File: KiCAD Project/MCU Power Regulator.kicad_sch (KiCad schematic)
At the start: 0 parts

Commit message: V1.0.0.0
Final version 1, sent for fabrication.
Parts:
- added C3: 10µF, Capacitor_SMD:C_0603_1608Metric, symbol Device:C
- added C4: 100n, Capacitor_SMD:C_0603_1608Metric, symbol Device:C
- added C5: 3n3, Capacitor_SMD:C_0603_1608Metric, symbol Device:C
- added C6: 22µ, Capacitor_SMD:C_0603_1608Metric, symbol Device:C
- added L2: VLS5045EX-2R2N, VLS5045EX330M, symbol 1016:VLS5045EX-2R2N
- added R3: 100K, Resistor_SMD:R_0603_1608Metric, symbol Device:R_US
- added R4: 31K6, Resistor_SMD:R_0603_1608Metric, symbol Device:R_US
- added R5: 1K6, Resistor_SMD:R_0603_1608Metric, symbol Device:R_US
- added TP1: TestPoint, TestPoint:TestPoint_THTPad_D1.0mm_Drill0.5mm, symbol Connector:TestPoint
- added U1: TPS62130RGTR, QFN50P300X300X100-17N-D, symbol 1016:TPS62130RGTR
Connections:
- net GND: now also C3.2, C4.2, C5.1, C6.2, R4.2, R5.1, U1.15 (PGND_1), U1.16 (PGND_2), U1.17 (EP), U1.6 (AGND), U1.8 (DEF)
- net VCC: now also C3.1, C4.1, U1.10 (AVIN), U1.11 (PVIN_1), U1.12 (PVIN_2), U1.13 (EN), U1.7 (FSW)
- new net MCUReg_FB: R3.2, R4.1, U1.5 (FB)
- new net MCUReg_SS: C5.2, U1.9 (SS/TR)
- new net MCUReg_Sw_Out: L2.1, U1.1 (SW_1), U1.2 (SW_2), U1.3 (SW_3)
- new net Vmcu: C6.1, L2.2, R3.1, R5.2, TP1.1, U1.14 (VOS)
- no-connect marks 0 -> 1
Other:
- note added: "3V3 Out for MCU"
- note added: "Inductor and Feedback"
- note added: "Input Filter"
- note added: "Power In 7V - 17V"
- note added: "Switching Regulator"

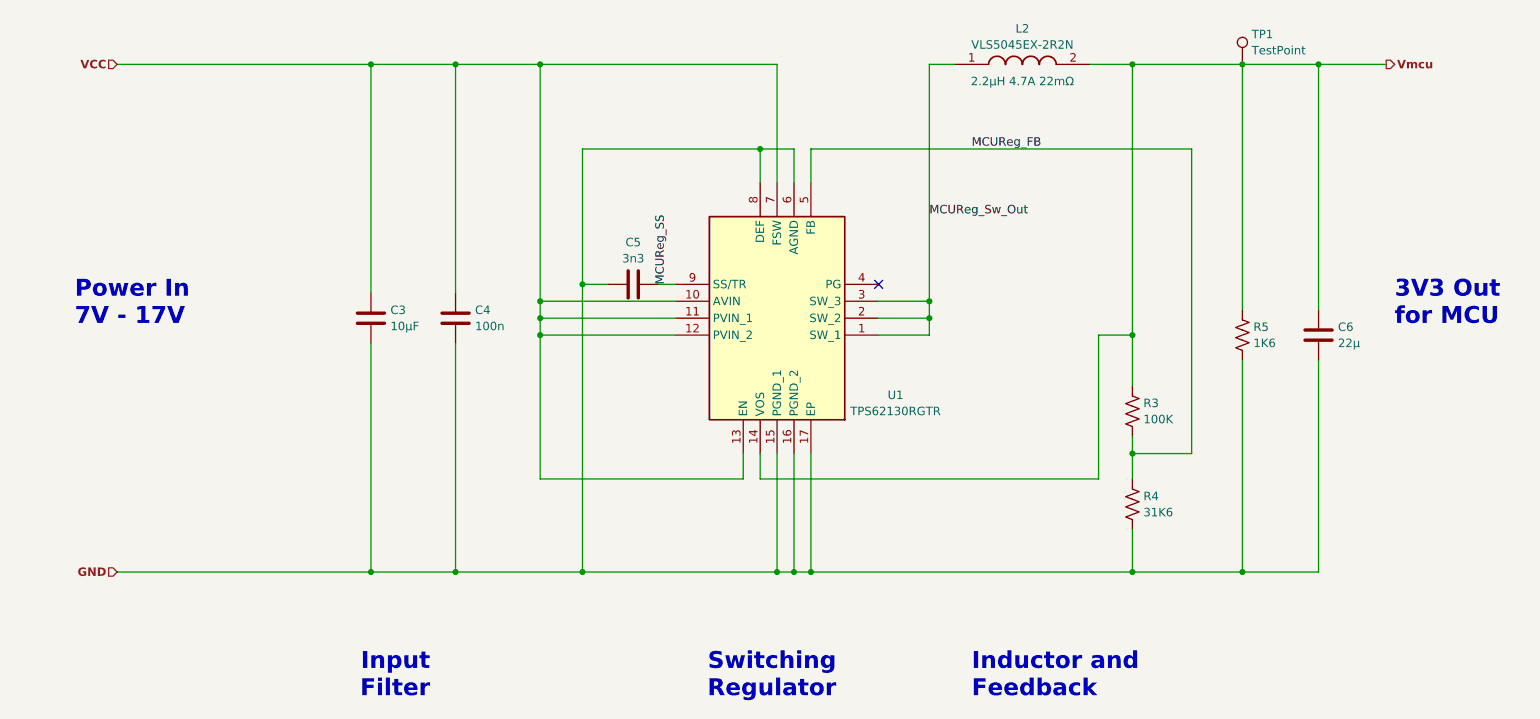
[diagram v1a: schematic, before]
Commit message: v2.0.0.0
1016 Breadboard Power Supply v2

- Change FSW connection to the Vout on all regulators
- Change regulator to TPS62130A so that PG pin goes low on thermal shutdown and UVLO
- Change PG pullup to be a resistor at the regulator vice pullup within STM32 so that it can be actively discharged
- Remove resistor across rail outputs for discharging to improve efficiency
- Change board dimensions to correct span
- Change pinout of STM32 for better routing
- Change Tag-Connect footprint to momentary connection (no legs)
- Make sure Tag-Connect footprint doesn't have solder paste layer
- Added heat sinks on bottom under rail regulators, added thermal vias
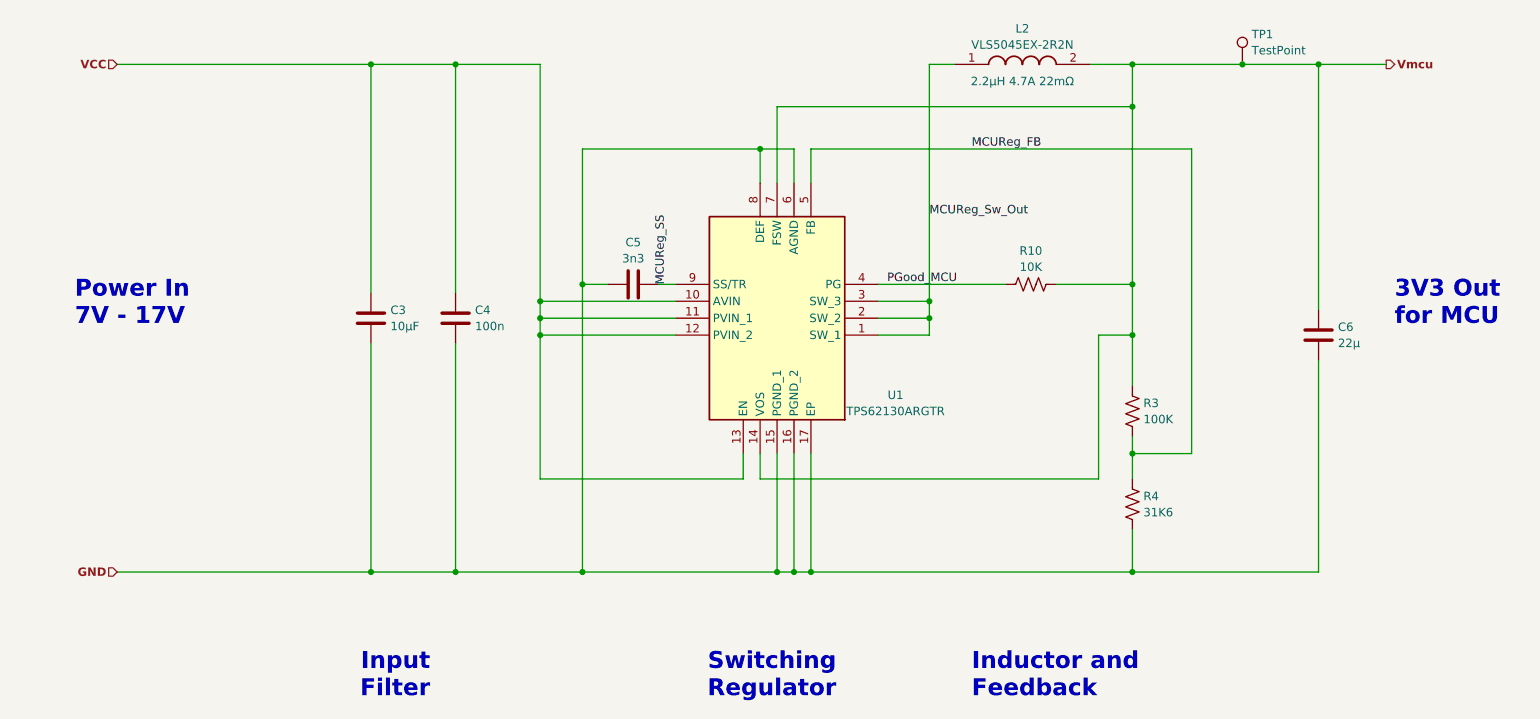
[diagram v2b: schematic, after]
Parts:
- removed R5: 1K6, Resistor_SMD:R_0603_1608Metric, symbol Device:R_US
- added R10: 10K, Resistor_SMD:R_0603_1608Metric, symbol Device:R_US
- U1: value TPS62130RGTR -> TPS62130ARGTR; LCSC Part Number C43590 -> C337502; Manufacturer_Part_Number TPS62130RGTR -> TPS62130ARGTR; Mouser Part Number 595-TPS62130RGTR -> 595-TPS62130ARGTR
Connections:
- net VCC: no longer U1.7 (FSW)
- net Vmcu: now also U1.7 (FSW), R10.2
- net PGood_MCU: now reaches U1.4 (PG)
- net PGood_MCU: now also R10.1
- no-connect marks 1 -> 0
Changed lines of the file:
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@@
   (junction (at 168.91 95.25) (diameter 0) (color 0 0 0 0)
   )
-  (junction (at 215.9 133.35) (diameter 0) (color 0 0 0 0)
-  )
   (junction (at 215.9 57.15) (diameter 0) (color 0 0 0 0)
   )
   (junction (at 199.39 115.57) (diameter 0) (color 0 0 0 0)
   )
-  (junction (at 110.49 57.15) (diameter 0) (color 0 0 0 0)
+  (junction (at 199.39 63.5) (diameter 0) (color 0 0 0 0)
   )
   (junction (at 151.13 133.35) (diameter 0) (color 0 0 0 0)
@@
   (junction (at 168.91 92.71) (diameter 0) (color 0 0 0 0)
   )
+  (junction (at 199.39 90.17) (diameter 0) (color 0 0 0 0)
+  )
   (junction (at 143.51 69.85) (diameter 0) (color 0 0 0 0)
   )
@@
   (junction (at 199.39 133.35) (diameter 0) (color 0 0 0 0)
   )
-  (no_connect (at 161.29 90.17))
   (wire (pts (xy 194.31 119.38) (xy 194.31 97.79))
     (stroke (width 0) (type default))
@@
     (stroke (width 0) (type default))
   )
-  (wire (pts (xy 215.9 133.35) (xy 227.33 133.35))
+  (wire (pts (xy 199.39 133.35) (xy 227.33 133.35))
+    (stroke (width 0) (type default))
+  )
+  (wire (pts (xy 146.05 74.93) (xy 146.05 63.5))
     (stroke (width 0) (type default))
   )
@@
     (stroke (width 0) (type default))
   )
-  (wire (pts (xy 215.9 101.6) (xy 215.9 133.35))
+  (wire (pts (xy 199.39 90.17) (xy 199.39 97.79))
     (stroke (width 0) (type default))
   )
@@
     (stroke (width 0) (type default))
   )
-  (wire (pts (xy 146.05 57.15) (xy 110.49 57.15))
-    (stroke (width 0) (type default))
-  )
   (wire (pts (xy 143.51 119.38) (xy 194.31 119.38))
     (stroke (width 0) (type default))
   )
+  (wire (pts (xy 199.39 63.5) (xy 199.39 90.17))
+    (stroke (width 0) (type default))
+  )
   (wire (pts (xy 146.05 133.35) (xy 148.59 133.35))
     (stroke (width 0) (type default))
@@
     (stroke (width 0) (type default))
   )
+  (wire (pts (xy 187.96 90.17) (xy 199.39 90.17))
+    (stroke (width 0) (type default))
+  )
+  (wire (pts (xy 161.29 90.17) (xy 180.34 90.17))
+    (stroke (width 0) (type default))
+  )
   (wire (pts (xy 199.39 97.79) (xy 199.39 105.41))
     (stroke (width 0) (type default))
@@
     (stroke (width 0) (type default))
   )
-  (wire (pts (xy 215.9 57.15) (xy 215.9 93.98))
-    (stroke (width 0) (type default))
-  )
   (wire (pts (xy 97.79 99.06) (xy 97.79 133.35))
     (stroke (width 0) (type default))
@@
     (stroke (width 0) (type default))
   )
-  (wire (pts (xy 199.39 133.35) (xy 215.9 133.35))
-    (stroke (width 0) (type default))
-  )
   (wire (pts (xy 148.59 69.85) (xy 143.51 69.85))
     (stroke (width 0) (type default))
   )
+  (wire (pts (xy 146.05 63.5) (xy 199.39 63.5))
+    (stroke (width 0) (type default))
+  )
   (wire (pts (xy 110.49 92.71) (xy 130.81 92.71))
     (stroke (width 0) (type default))
   )
-  (wire (pts (xy 146.05 74.93) (xy 146.05 57.15))
-    (stroke (width 0) (type default))
-  )
   (wire (pts (xy 199.39 113.03) (xy 199.39 115.57))
     (stroke (width 0) (type default))
@@
     (stroke (width 0) (type default))
   )
-  (wire (pts (xy 199.39 57.15) (xy 199.39 97.79))
+  (wire (pts (xy 199.39 57.15) (xy 199.39 63.5))
     (stroke (width 0) (type default))
   )
@@
   )
   (label "MCUReg_SS" (at 129.54 90.17 90) (fields_autoplaced)
+    (effects (font (size 1.27 1.27)) (justify left bottom))
+  )
+  (label "PGood_MCU" (at 162.56 90.17 0) (fields_autoplaced)
     (effects (font (size 1.27 1.27)) (justify left bottom))
   )
@@
     )
   )
-  (symbol (lib_id "Device:R_US") (at 215.9 97.79 180) (unit 1)
-    (in_bom yes) (on_board yes) (dnp no) (fields_autoplaced)
-    (property "Reference" "R5" (at 217.551 96.5779 0)
-      (effects (font (size 1.27 1.27)) (justify right))
-    )
-    (property "Value" "1K6" (at 217.551 99.0021 0)
-      (effects (font (size 1.27 1.27)) (justify right))
-    )
-    (property "Footprint" "Resistor_SMD:R_0603_1608Metric" (at 214.884 97.536 90)
-      (effects (font (size 1.27 1.27)) hide)
-    )
-    (property "Datasheet" "https://www.mouser.com/datasheet/2/447/YAGEO_PYu_RC_Group_51_RoHS_L_12-3313492.pdf" (at 215.9 97.79 0)
-      (effects (font (size 1.27 1.27)) hide)
-    )
-    (property "Description" "Output Discharge Resistor" (at 215.9 97.79 0)
-      (effects (font (size 1.27 1.27)) hide)
-    )
-    (property "Height" "0.45" (at 215.9 97.79 0)
-      (effects (font (size 1.27 1.27)) hide)
-    )
-    (property "LCSC Part Number" "C165489" (at 215.9 97.79 0)
-      (effects (font (size 1.27 1.27)) hide)
-    )
-    (property "Manufacturer_Name" "Yageo" (at 215.9 97.79 0)
-      (effects (font (size 1.27 1.27)) hide)
-    )
-    (property "Manufacturer_Part_Number" "RC0603FR-071K6L" (at 215.9 97.79 0)
-      (effects (font (size 1.27 1.27)) hide)
-    )
-    (property "Mouser Part Number" "603-RC0603FR-071K6L" (at 215.9 97.79 0)
-      (effects (font (size 1.27 1.27)) hide)
-    )
-    (property "Spec" "1K6 100mW" (at 215.9 97.79 0)
-      (effects (font (size 1.27 1.27)) hide)
-    )
-    (pin "1")
-    (pin "2")
-    (instances
-      (project "1016 Breadboard Power Supply"
-        (path "/f4b22203-0926-4e3a-b453-85f22789c08a/280adcb7-ede6-4688-bc7e-541657c4a091"
-          (reference "R5") (unit 1)
-        )
-      )
-    )
-  )
   (symbol (lib_id "Device:C") (at 97.79 95.25 0) (unit 1)
     (in_bom yes) (on_board yes) (dnp no) (fields_autoplaced)
@@
       (effects (font (size 1.27 1.27)))
     )
-    (property "Value" "TPS62130RGTR" (at 163.83 109.22 0)
+    (property "Value" "TPS62130ARGTR" (at 163.83 109.22 0)
       (effects (font (size 1.27 1.27)))
     )
@@
       (effects (font (size 1.27 1.27)) (justify left top) hide)
     )
-    (property "Manufacturer_Part_Number" "TPS62130RGTR" (at 134.62 -486.97 0)
-      (effects (font (size 1.27 1.27)) (justify left top) hide)
-    )
-    (property "Mouser Part Number" "595-TPS62130RGTR" (at 134.62 -586.97 0)
+    (property "Manufacturer_Part_Number" "TPS62130ARGTR" (at 134.62 -486.97 0)
+      (effects (font (size 1.27 1.27)) (justify left top) hide)
+    )
+    (property "Mouser Part Number" "595-TPS62130ARGTR" (at 134.62 -586.97 0)
       (effects (font (size 1.27 1.27)) (justify left top) hide)
     )
@@
       (effects (font (size 1.27 1.27)) hide)
     )
-    (property "LCSC Part Number" "C43590" (at 161.29 97.79 0)
+    (property "LCSC Part Number" "C337502" (at 161.29 97.79 0)
       (effects (font (size 1.27 1.27)) hide)
     )
@@
         )
       )
+    )
+  )
+  (symbol (lib_id "Device:R_US") (at 184.15 90.17 90) (unit 1)
+    (in_bom yes) (on_board yes) (dnp no) (fields_autoplaced)
+    (property "Reference" "R10" (at 184.15 85.1367 90)
+      (effects (font (size 1.27 1.27)))
+    )
+    (property "Value" "10K" (at 184.15 87.5609 90)
+      (effects (font (size 1.27 1.27)))
+    )
+    (property "Footprint" "Resistor_SMD:R_0603_1608Metric" (at 184.404 89.154 90)
+      (effects (font (size 1.27 1.27)) hide)
+    )
+    (property "Datasheet" "https://www.mouser.com/datasheet/2/447/YAGEO_PYu_RC_Group_51_RoHS_L_12-3313492.pdf" (at 184.15 90.17 0)
+      (effects (font (size 1.27 1.27)) hide)
+    )
+    (property "Description" "Power Good Pull-Up Resistor" (at 184.15 90.17 0)
+      (effects (font (size 1.27 1.27)) hide)
+    )
+    (property "Height" "0.45" (at 184.15 90.17 0)
+      (effects (font (size 1.27 1.27)) hide)
+    )
+    (property "LCSC Part Number" "C98220" (at 184.15 90.17 0)
+      (effects (font (size 1.27 1.27)) hide)
+    )
+    (property "Manufacturer_Name" "Yageo" (at 184.15 90.17 0)
+      (effects (font (size 1.27 1.27)) hide)
+    )
+    (property "Manufacturer_Part_Number" "RC0603FR-0710KL" (at 184.15 90.17 0)
+      (effects (font (size 1.27 1.27)) hide)
+    )
+    (property "Mouser Part Number" "603-RC0603FR-0710KL" (at 184.15 90.17 0)
+      (effects (font (size 1.27 1.27)) hide)
+    )
+    (property "Spec" "10K 100mW" (at 184.15 90.17 0)
+      (effects (font (size 1.27 1.27)) hide)
+    )
+    (pin "1")
+    (pin "2")
+    (instances
+      (project "1016 Breadboard Power Supply"
+        (path "/f4b22203-0926-4e3a-b453-85f22789c08a/280adcb7-ede6-4688-bc7e-541657c4a091"
+          (reference "R10") (unit 1)
+        )
+      )
